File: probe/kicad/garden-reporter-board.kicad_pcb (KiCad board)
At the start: 2 copper layers, 40.6 x 88.9 mm, 26 parts, among them J1 70543-0106, J2 Conn_01x02, J3 70543-0002, J4 70543-0002, J5 70543-0002, Q1 TN0702N3-G, U1 MCP1700-3302E_TO92, U2 MCP1700-3302E_TO92, U3 MCP1700-1202E_TO92

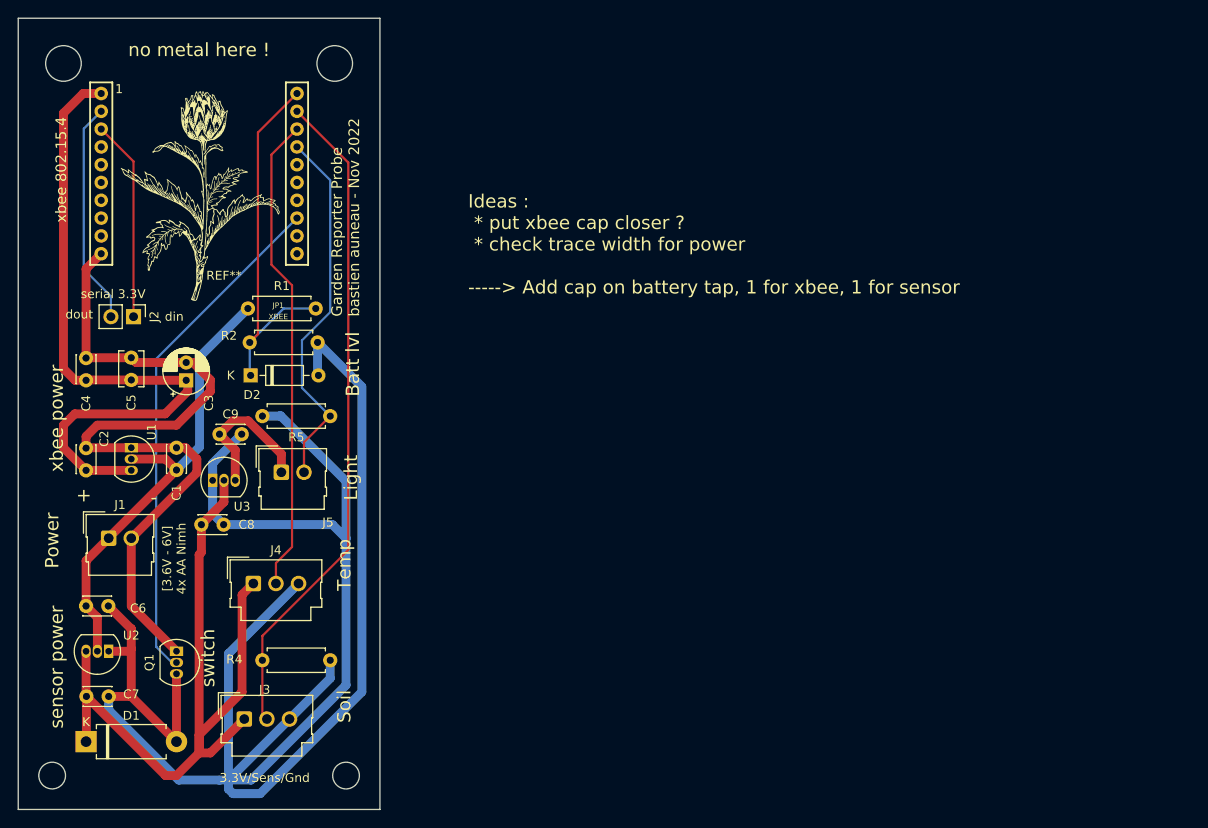
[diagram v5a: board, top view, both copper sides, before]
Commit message: Add ceriamic cap for xbee and heavy load sensors, better routing of voltage regulator capacitors, more compact outline
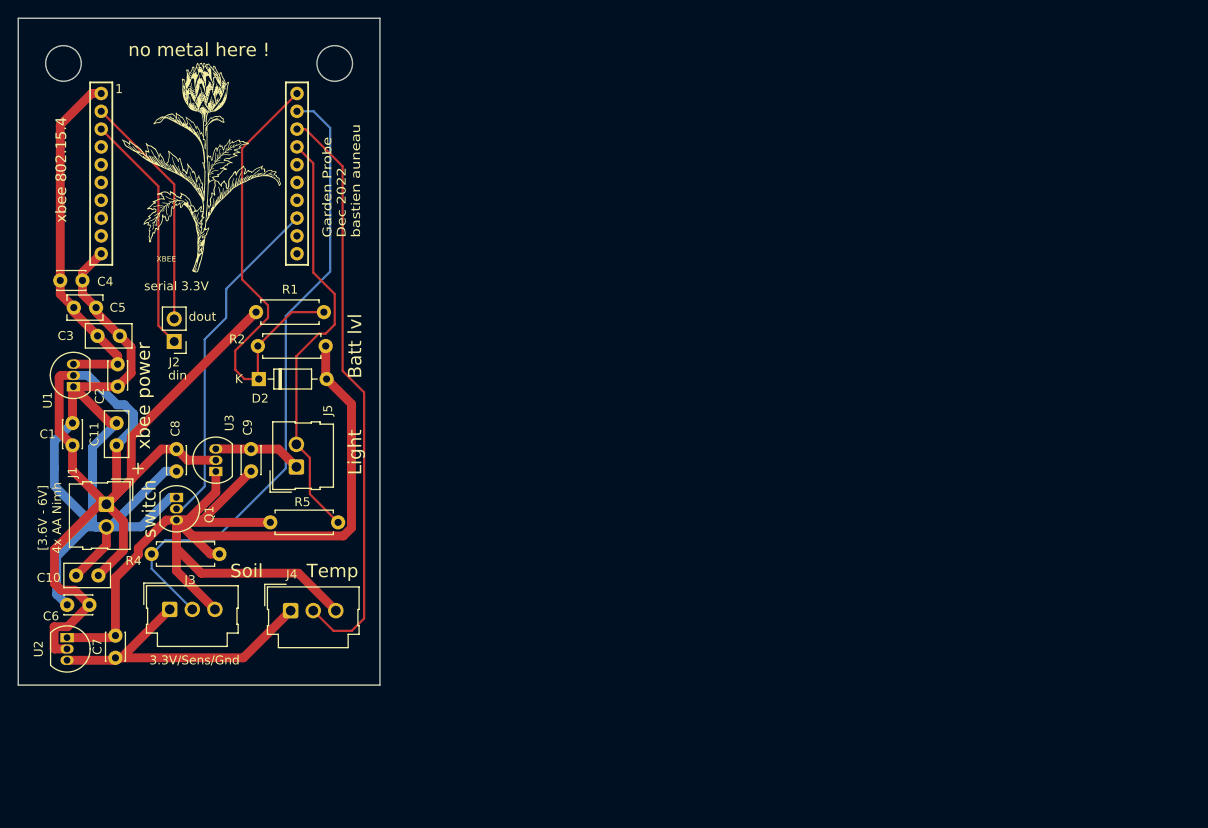
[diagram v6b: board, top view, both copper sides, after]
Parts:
- removed D1: SB130, Diode_THT:D_DO-15_P10.16mm_Horizontal
- added C10: 10uF, Capacitor_THT:C_Disc_D5.0mm_W2.5mm_P2.50mm, F.Cu at (142.3, 117.2)
- added C11: 10uF, Capacitor_THT:C_Disc_D5.0mm_W2.5mm_P2.50mm, F.Cu at (144.4, 102.6)
- added G***: LOGO, LOGO, B.Cu at (153.3, 71.5)
- C3: footprint Capacitor_THT:CP_Radial_D5.0mm_P2.00mm -> Capacitor_THT:C_Disc_D5.0mm_W2.5mm_P2.50mm
- moved Q1 17.3 mm to (151.1, 108.5)
- moved R4 17.2 mm to (148.3, 114.8)
- moved J3 14.9 mm to (150.4, 121.0)
- moved C2 12.4 mm to (144.5, 93.5), turned to -90 degrees
- moved C1 12.0 mm to (139.4, 102.6)
- moved R5 12.0 mm to (169.3, 111.3)
- moved C4 11.6 mm to (138.1, 84.1), turned to 0 degrees
- moved C3 11.1 mm to (142.3, 90.3), turned to 0 degrees
- moved C5 10.4 mm to (139.6, 87.1), turned to 0 degrees
- moved U1 9.45 mm to (139.6, 96.0), turned to 90 degrees
- moved C8 8.94 mm to (151.1, 103.0), turned to -90 degrees
- moved C7 5.43 mm to (144.3, 126.5), turned to 90 degrees
- moved J2 5.36 mm to (150.9, 90.9), turned to 180 degrees
- moved J4 5.18 mm to (164.0, 121.2)
- moved U2 4.92 mm to (138.8, 124.2), turned to -90 degrees
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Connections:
- C6 pad 2: GND1 -> -BATT
- C8 pad 1: +3.3VADC -> +BATT
- C8 pad 2: GND1 -> -BATT
- U3 pad 2: +3.3VADC -> +BATT
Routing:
- net GND1: track 238.2 -> 136.0 mm
- net +BATT: track 52.2 -> 117.6 mm
- net +3.3VADC: track 87.6 -> 35.8 mm
- net +3.3V: track 76.3 -> 40.6 mm
- net /xbee_ON: track 57.7 -> 38.7 mm
- net -BATT: track 85.8 -> 102.4 mm
- net /sensor_temp: track 54.0 -> 65.9 mm
- net /sensor_batt: track 42.9 -> 52.2 mm
- net +1V2: track 17.1 -> 9.89 mm
- net /sensor_light: track 42.0 -> 48.1 mm
- net Net-(J2-Pad1): track 22.6 -> 27.3 mm
- net /sensor_soil: track 74.9 -> 72.0 mm
- net Net-(J2-Pad2): track 25.1 -> 26.7 mm
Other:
- board size 40.6 x 88.9 mm -> 40.6 x 74.9 mm
- board text added: "Garden Probe Dec 2022 bastien auneau"
- board text removed: "-"
- board text removed: "Garden Reporter Probe bastien auneau - Nov 2022"
- board text removed: "Ideas : * put xbee cap closer ? * check trace width for power -----> Add cap on battery tap, 1 for xbee, 1 for sensor"
- board text removed: "Power"
- board text removed: "sensor power"

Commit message: Routing decouple cap
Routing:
- net GND1: track 136.0 -> 141.3 mm
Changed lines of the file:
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@@
   (segment (start 142.6718 63.06566) (end 141.59417 63.06566) (width 1) (layer "F.Cu") (net 3))
   (segment (start 138.069 85.598) (end 139.593 87.122) (width 1) (layer "F.Cu") (net 3))
+  (segment (start 140.582 124.206) (end 146.558 118.23) (width 1) (layer "F.Cu") (net 4))
   (segment (start 167.9956 95.1484) (end 170.791 97.9438) (width 1) (layer "F.Cu") (net 4))
   (segment (start 155.554 107.874) (end 152.43 110.998) (width 1) (layer "F.Cu") (net 4))
@@
   (segment (start 167.894 91.44) (end 167.894 95.0468) (width 1) (layer "F.Cu") (net 4))
   (segment (start 161.671 111.252) (end 151.384 111.252) (width 1) (layer "F.Cu") (net 4))
+  (segment (start 148.844 110.998) (end 151.13 110.998) (width 1) (layer "F.Cu") (net 4))
   (segment (start 152.43 110.998) (end 151.13 110.998) (width 1) (layer "F.Cu") (net 4))
   (segment (start 159.512 105.517) (end 154.031 110.998) (width 1) (layer "F.Cu") (net 4))
-  (segment (start 144.272 117.475) (end 146.836 114.911) (width 1) (layer "F.Cu") (net 4))
   (segment (start 155.956 114.808) (end 154.94 114.808) (width 1) (layer "F.Cu") (net 4))
   (segment (start 151.13 116.713) (end 151.13 110.998) (width 1) (layer "F.Cu") (net 4))
@@
   (segment (start 164.834 116.967) (end 153.924 116.967) (width 1) (layer "F.Cu") (net 4))
   (segment (start 151.384 111.252) (end 151.13 110.998) (width 1) (layer "F.Cu") (net 4))
-  (segment (start 144.038 124.206) (end 144.272 123.972) (width 1) (layer "F.Cu") (net 4))
   (segment (start 169.888321 112.776) (end 152.908 112.776) (width 1) (layer "F.Cu") (net 4))
+  (segment (start 146.558 118.23) (end 146.558 121.686) (width 1) (layer "F.Cu") (net 4))
   (segment (start 155.554 105.537) (end 155.554 107.874) (width 1) (layer "F.Cu") (net 4))
-  (segment (start 146.836 114.911) (end 146.836 114.149) (width 1) (layer "F.Cu") (net 4))
-  (segment (start 144.272 123.972) (end 144.272 117.475) (width 1) (layer "F.Cu") (net 4))
+  (segment (start 146.558 113.284) (end 148.844 110.998) (width 1) (layer "F.Cu") (net 4))
   (segment (start 154.031 110.998) (end 151.13 110.998) (width 1) (layer "F.Cu") (net 4))
-  (segment (start 146.836 114.149) (end 149.987 110.998) (width 1) (layer "F.Cu") (net 4))
-  (segment (start 138.832 124.206) (end 144.038 124.206) (width 1) (layer "F.Cu") (net 4))
+  (segment (start 138.832 124.206) (end 140.582 124.206) (width 1) (layer "F.Cu") (net 4))
   (segment (start 169.037 121.17) (end 164.834 116.967) (width 1) (layer "F.Cu") (net 4))
-  (segment (start 149.987 110.998) (end 151.13 110.998) (width 1) (layer "F.Cu") (net 4))
   (segment (start 152.908 112.776) (end 151.13 110.998) (width 1) (layer "F.Cu") (net 4))
+  (segment (start 146.558 121.686) (end 144.272 123.972) (width 1) (layer "F.Cu") (net 4))
   (segment (start 170.791 111.873321) (end 169.888321 112.776) (width 1) (layer "F.Cu") (net 4))
   (segment (start 153.924 116.967) (end 151.13 114.173) (width 1) (layer "F.Cu") (net 4))
+  (segment (start 146.558 118.23) (end 146.558 113.284) (width 1) (layer "F.Cu") (net 4))
   (segment (start 170.791 97.9438) (end 170.791 111.873321) (width 1) (layer "F.Cu") (net 4))
   (segment (start 167.894 95.0468) (end 167.9956 95.1484) (width 1) (layer "F.Cu") (net 4))

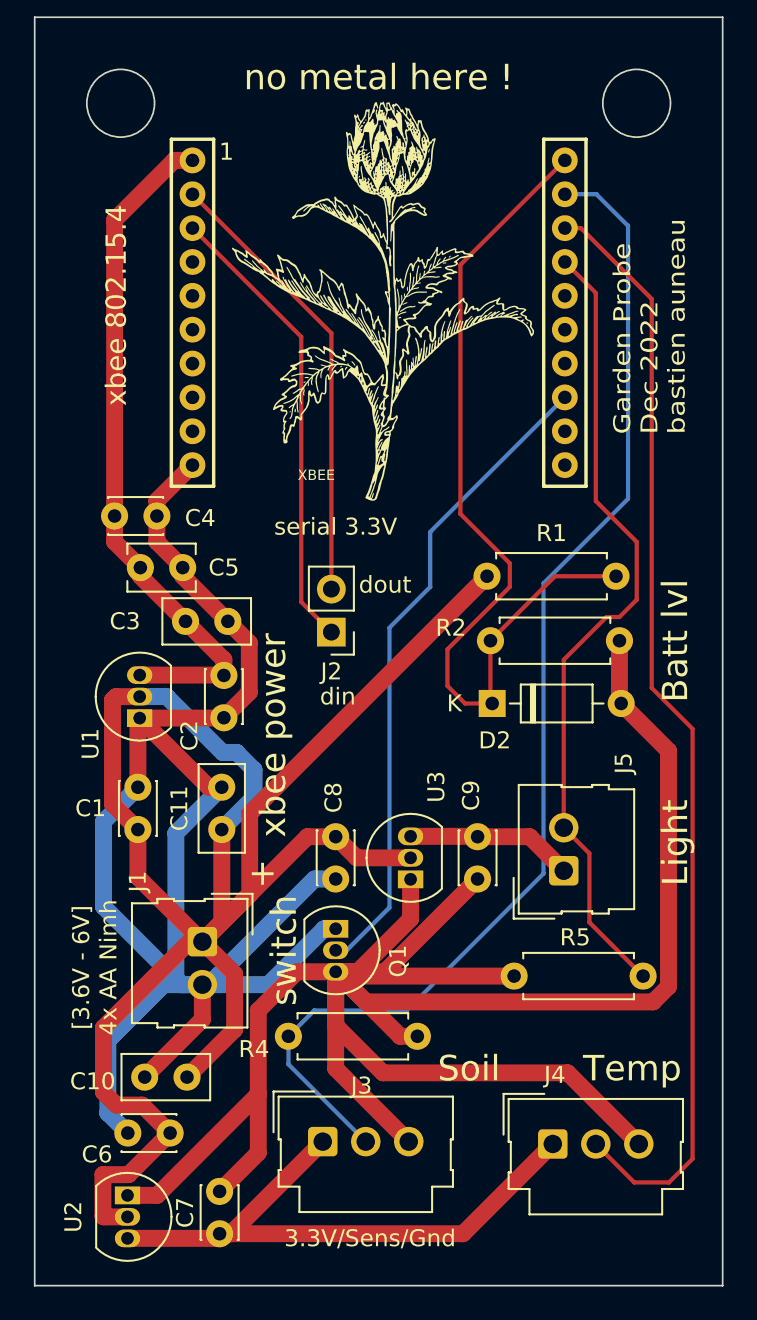
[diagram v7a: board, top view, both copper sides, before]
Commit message: Use high side switch, chose new components and footprints, layed out but no route, use GND plane, add doc and datasheet
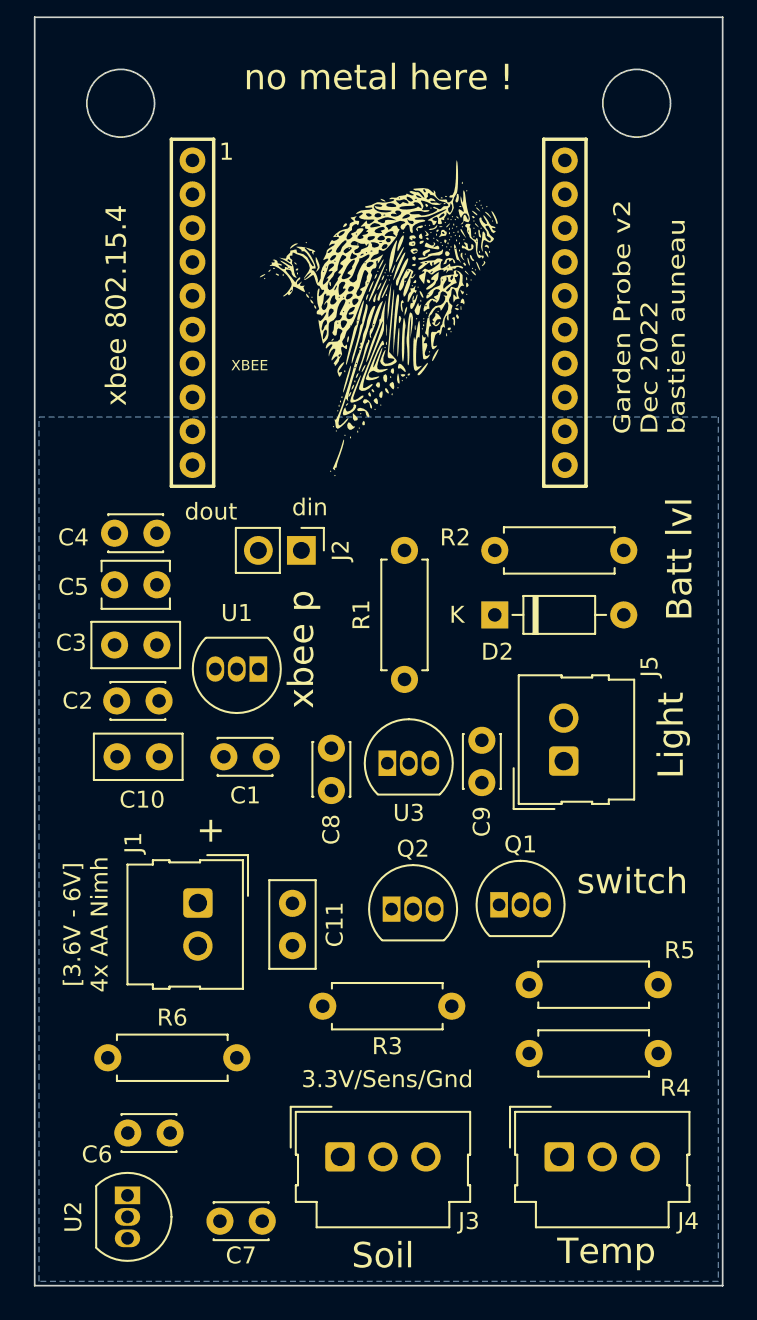
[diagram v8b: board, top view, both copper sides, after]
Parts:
- added Q2: Q_PMOS_SGD, Package_TO_SOT_THT:TO-92_Inline, F.Cu at (154.4, 107.3)
- added R3: 20K, Resistor_THT:R_Axial_DIN0207_L6.3mm_D2.5mm_P7.62mm_Horizontal, F.Cu at (158.0, 113.0)
- added R6: 10K, Resistor_THT:R_Axial_DIN0207_L6.3mm_D2.5mm_P7.62mm_Horizontal, F.Cu at (137.7, 116.1)
- G***: moved to F.Cu
- Q1: value TN0702N3-G -> Q_NMOS_SGD
- REF**: moved to B.Cu
- moved R4 21.9 mm to (170.2, 115.8), turned to 180 degrees
- moved C10 19.0 mm to (140.7, 98.3)
- moved Q1 9.76 mm to (160.8, 107.0), turned to 0 degrees
- moved R1 7.81 mm to (155.2, 93.7), turned to 90 degrees
- moved U1 7.58 mm to (146.6, 93.1), turned to 180 degrees
- moved U3 7.00 mm to (154.2, 98.7), turned to 0 degrees
- moved C1 6.65 mm to (144.5, 98.3), turned to 0 degrees
- moved C2 6.51 mm to (138.2, 95.0), turned to 0 degrees
- moved J5 6.48 mm to (164.6, 98.6)
- moved C11 6.04 mm to (148.6, 107.0), turned to -90 degrees
- moved R2 5.34 mm to (160.5, 86.1)
- moved D2 5.23 mm to (160.5, 89.9)
- moved C8 5.23 mm to (150.9, 97.8)
- moved J2 5.14 mm to (149.1, 86.1), turned to -90 degrees
- moved C3 4.42 mm to (138.1, 91.7)
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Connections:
- C6 pad 1: +BATT -> VDD
- C7 pad 2: GND1 -> -BATT
- C8 pad 1: +BATT -> VDD
- C9 pad 2: GND1 -> -BATT
- D2 pad 2: GND1 -> -BATT
- J3 pad 3: GND1 -> -BATT
- J4 pad 3: GND1 -> -BATT
- Q1 pad 3: GND1 -> Net-(R3-Pad1)
- R1 pad 1: +BATT -> VDD
- R2 pad 2: GND1 -> -BATT
- R4 pad 2: GND1 -> -BATT
- R5 pad 2: GND1 -> -BATT
- U2 pad 1: GND1 -> -BATT
- U2 pad 2: +BATT -> VDD
- U3 pad 1: GND1 -> -BATT
- U3 pad 2: +BATT -> VDD
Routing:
- net GND1: track 141.3 -> 0.00 mm
- net +BATT: track 117.6 -> 0.00 mm
- net -BATT: track 102.4 -> 0.00 mm
- net /sensor_soil: track 72.0 -> 0.00 mm
- net /sensor_temp: track 65.9 -> 0.00 mm
- net /sensor_batt: track 52.2 -> 0.00 mm
- net /sensor_light: track 48.1 -> 0.00 mm
- net +3.3V: track 40.6 -> 0.00 mm
- net /xbee_ON: track 38.7 -> 0.00 mm
- net +3.3VADC: track 35.8 -> 0.00 mm
- net Net-(J2-Pad1): track 27.3 -> 0.00 mm
- net Net-(J2-Pad2): track 26.7 -> 0.00 mm
- net +1V2: track 9.89 -> 0.00 mm
- added copper zone on B.Cu, net -BATT
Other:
- board text added: "Garden Probe v2 Dec 2022 bastien auneau"
- board text added: "xbee p"
- board text removed: "Garden Probe Dec 2022 bastien auneau"
- board text removed: "serial 3.3V"
- board text removed: "xbee power"
